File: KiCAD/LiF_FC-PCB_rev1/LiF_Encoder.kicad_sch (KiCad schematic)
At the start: 10 parts, among them J39 ENC 3V3_{EN}, U16 SN74HC14DR

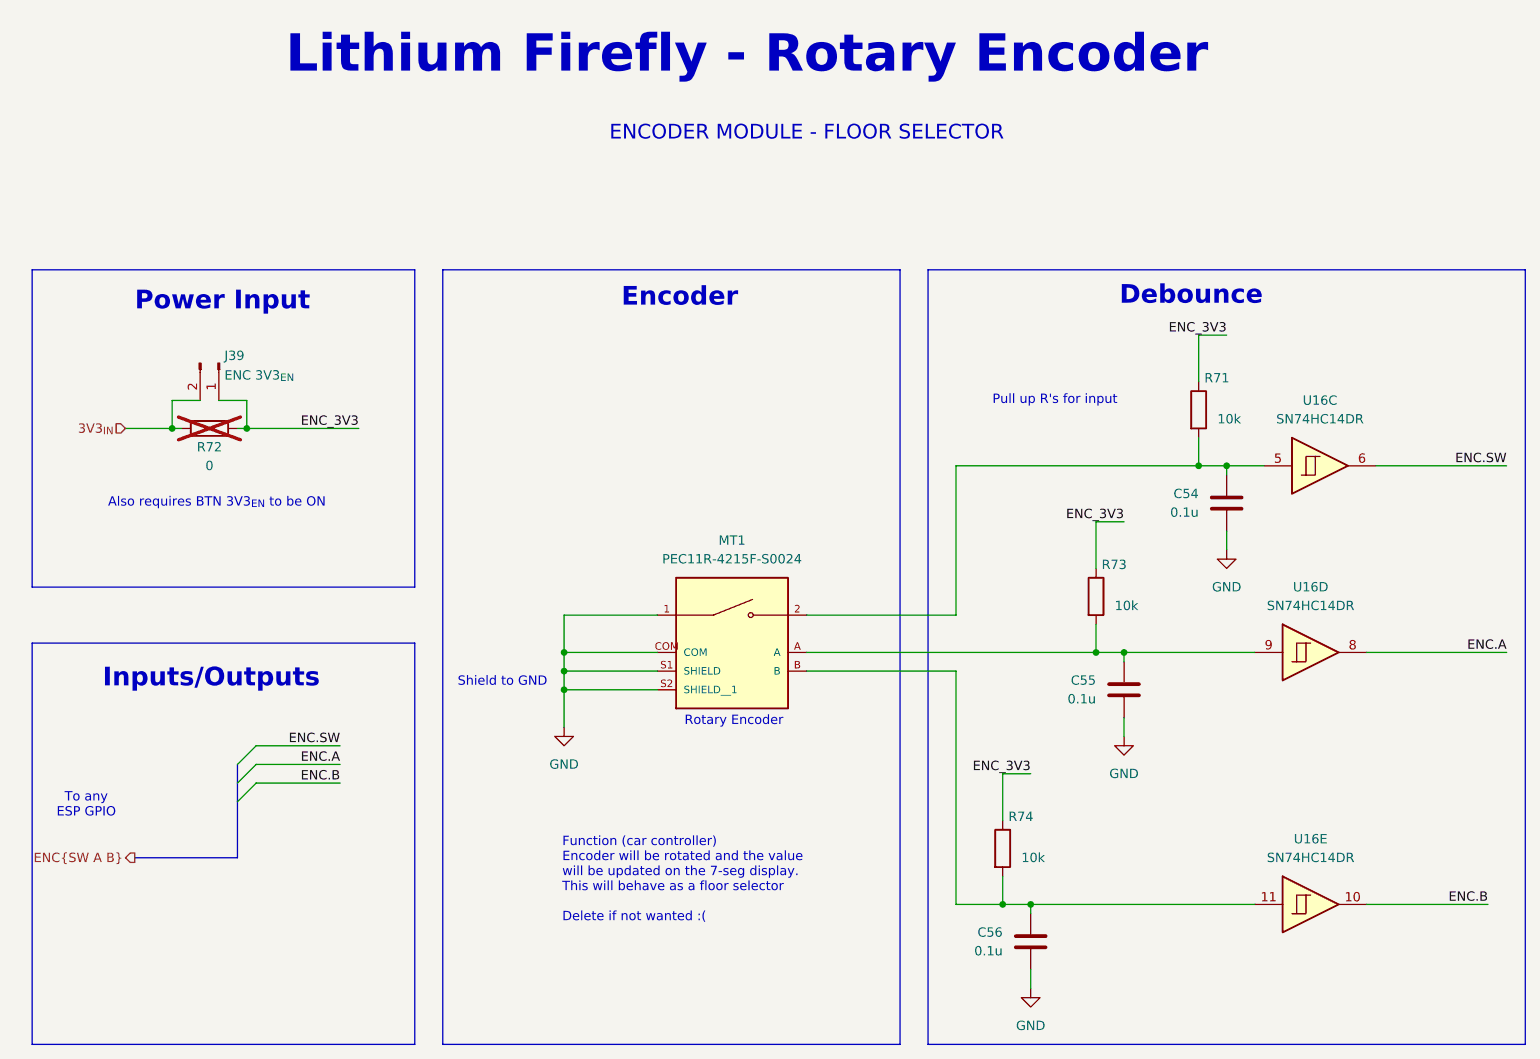
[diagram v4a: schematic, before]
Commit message: Created new KiCAD project for IO PCB, moved relevant components there, saving backup before reannotating the Service PCB schematics
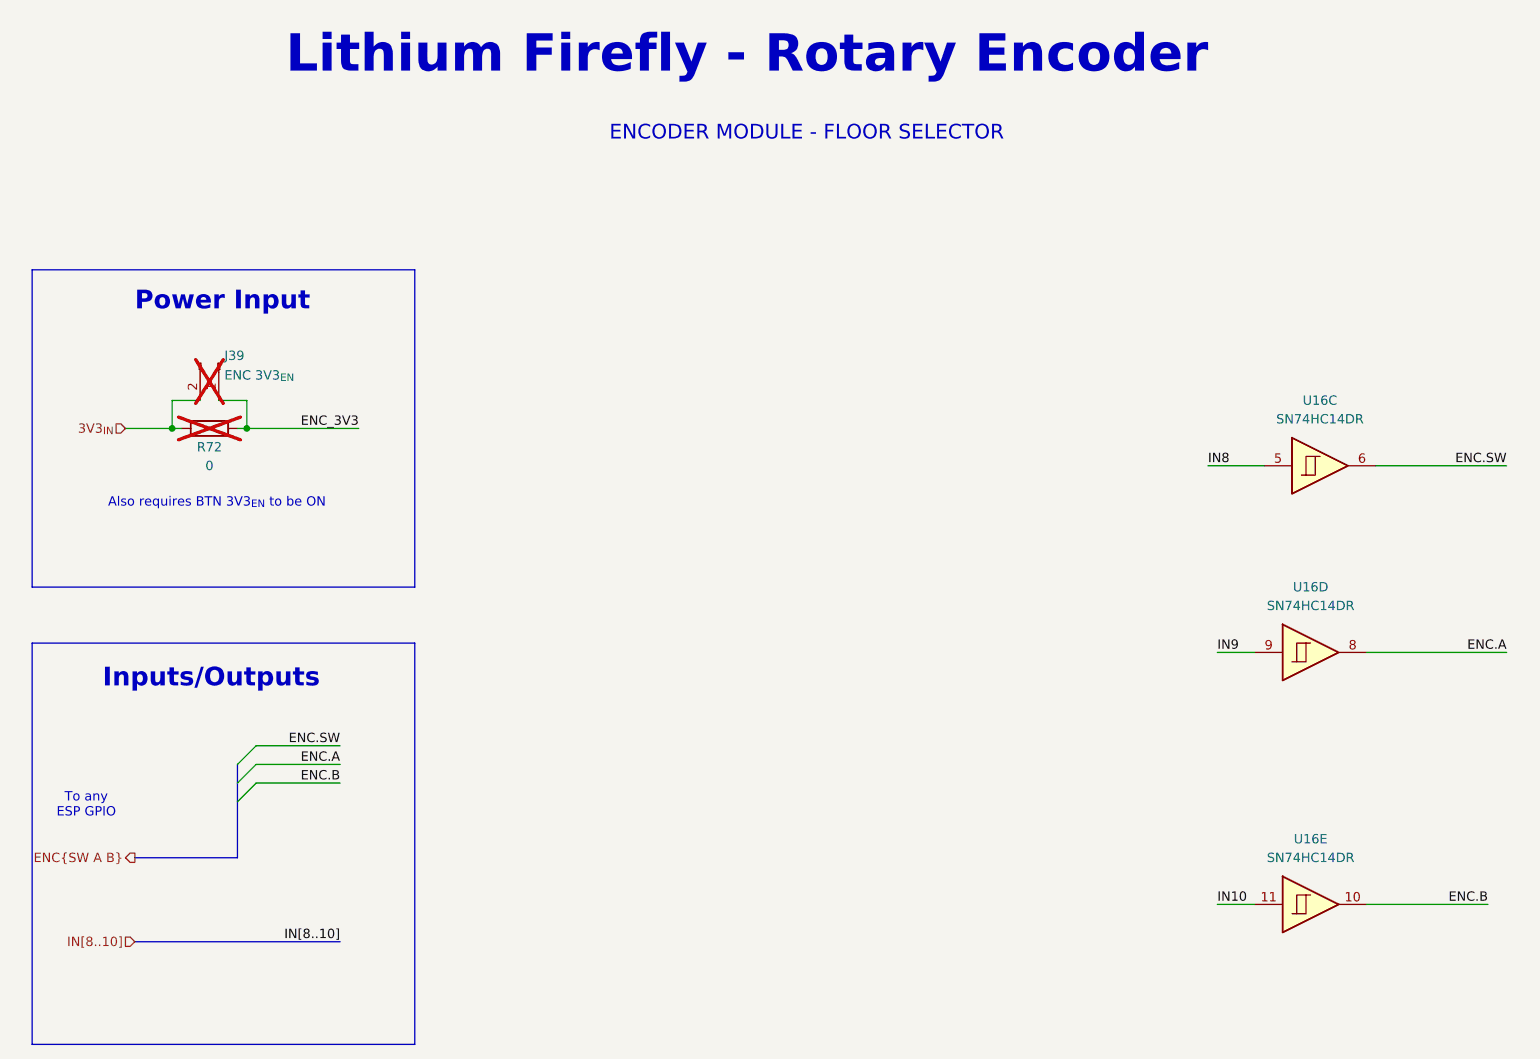
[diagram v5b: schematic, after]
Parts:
- removed C54, C55, C56: 0.1u, Capacitor_SMD:C_0805_2012Metric, symbol Device:C
- removed MT1: PEC11R-4215F-S0024, LiF_PCB_Footprints:XDCR_PEC11R-4215F-S0024, symbol LiF_PCB_Symbols:PEC11R-4215F-S0024
- removed R71, R73, R74: 10k, Resistor_SMD:R_0805_2012Metric, symbol Device:R
- J39: now not fitted; now left out of the parts list
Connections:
- net IN8: now reaches U16.5
- net IN10: now reaches U16.11
- net IN9: now reaches U16.9
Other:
- note removed: "Debounce"
- note removed: "Encoder"
- note removed: "Function (car controller) Encoder will be rotated and the value will be updated on the 7-seg display. This will behave as a floor selector Delete if not wanted :("
- note removed: "Pull up R's for input"
- note removed: "Rotary Encoder"
- note removed: "Shield to GND"

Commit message: backup before redoing the analog section
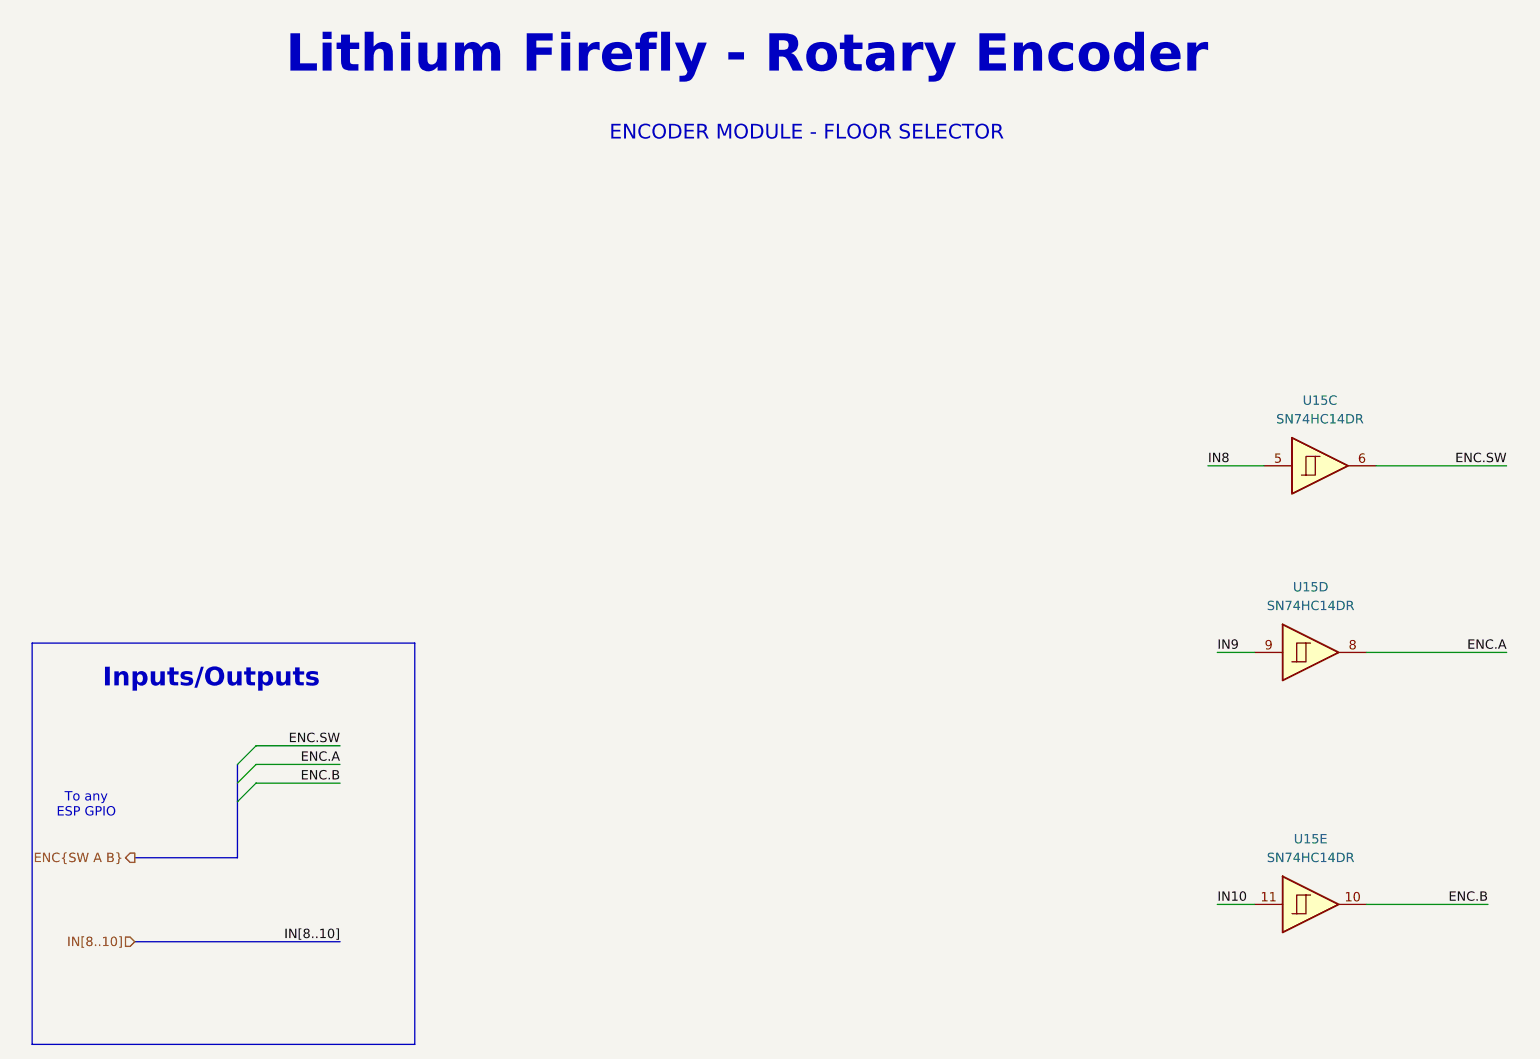
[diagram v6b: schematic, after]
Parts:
- removed J39: ENC 3V3_{EN}, Connector_PinHeader_2.54mm:PinHeader_1x02_P2.54mm_Vertical_SMD_Pin1Left, symbol Connector:Conn_01x02_Pin
- removed R72: 0, Resistor_SMD:R_0805_2012Metric, symbol Device:R
- renumbered U16 to U15
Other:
- note removed: "Also requires BTN 3V3_{EN} to be ON"
- note removed: "Power Input"
